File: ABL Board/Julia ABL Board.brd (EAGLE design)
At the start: 62.2 x 63.5 mm, 32 parts, among them Q1 MMBT4403, U2 LM317, U5 HX711, X1 LOADCELL 3, X2 LOADCELL 2, X3 LOADCELL 1, X4 INPUT, X8 ABL_LED

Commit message: generated ABL board gerbers
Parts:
- added U$2: FRACKTALLOGO, FracktalWorks_Eagle_Library:FRACKTALLOGO
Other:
- board text added: "Julia ABL Board V1.1"
- board text added: "Solder jumper for 12V operation"
- board text removed: "Julia ABL Board V1"
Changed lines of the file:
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@@
 <board>
 <plain>
-<wire x1="57.15" y1="88.9" x2="106.68" y2="88.9" width="0.1524" layer="51"/>
-<wire x1="106.68" y1="88.9" x2="106.68" y2="35.56" width="0.1524" layer="51"/>
-<wire x1="106.68" y1="35.56" x2="57.15" y2="35.56" width="0.1524" layer="51"/>
-<wire x1="57.15" y1="35.56" x2="57.15" y2="88.9" width="0.1524" layer="51"/>
 <hole x="57.15" y="88.9" drill="3"/>
 <hole x="106.68" y="88.9" drill="3"/>
@@
 <wire x1="50.8" y1="35.56" x2="50.8" y2="88.9" width="0.1524" layer="20"/>
 <wire x1="113.03" y1="35.56" x2="107.95" y2="30.48" width="0.1524" layer="20" curve="-90"/>
-<text x="71.12" y="33.02" size="1.778" layer="27">Julia ABL Board V1</text>
+<text x="70.5866" y="90.3478" size="1.778" layer="27">Julia ABL Board V1.1</text>
+<text x="82.5754" y="87.3506" size="1.016" layer="25">Solder jumper for 12V operation</text>
 </plain>
 <attributes>
@@
 <attribute name="VALUE" x="76.2" y="36.703" size="0.0254" layer="27"/>
 </element>
+<element name="U$2" library="FracktalWorks_Eagle_Library" package="FRACKTALLOGO" value="FRACKTALLOGO" x="79.502" y="32.1056" smashed="yes"/>
 </elements>
 <signals>
@@
 <mfgpreviewcolor name="substratecolor" color="0xFF786E46"/>
 </mfgpreviewcolors>
+<errors>
+</errors>
 </board>
 </drawing>

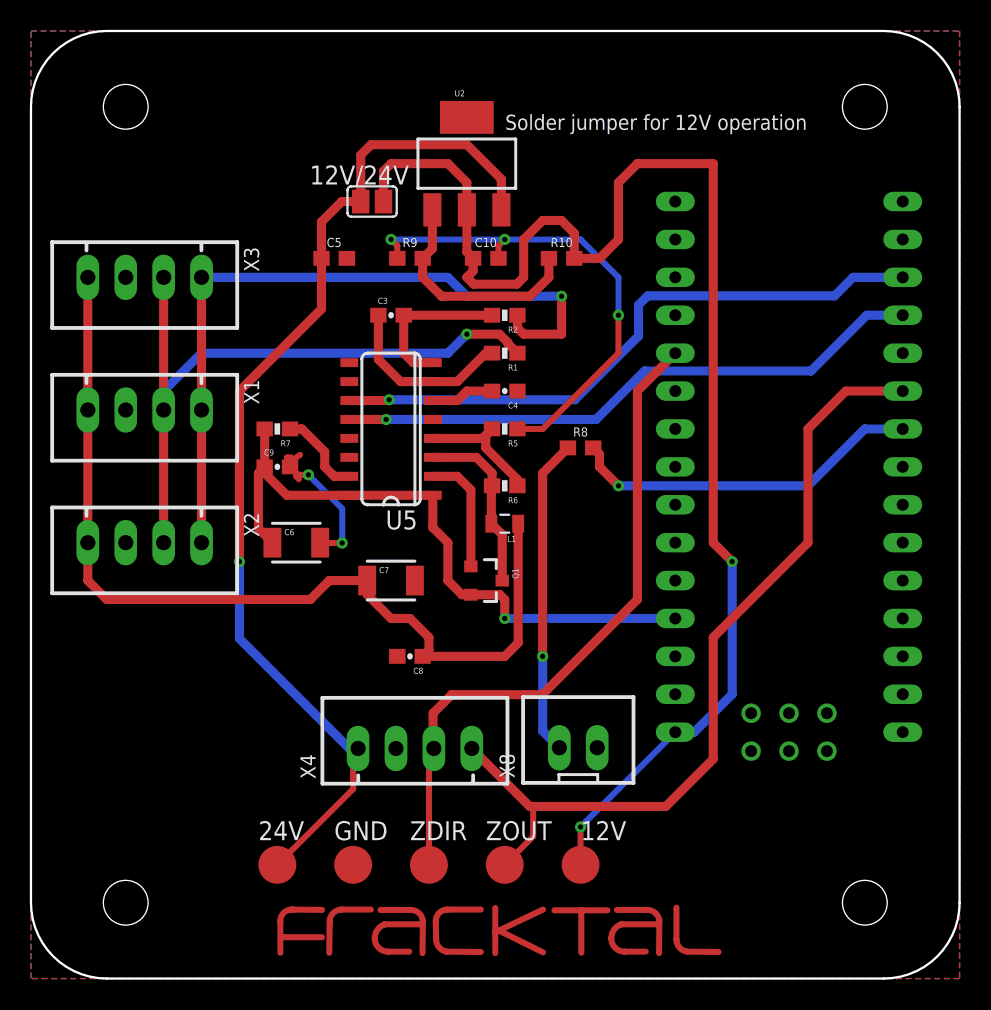
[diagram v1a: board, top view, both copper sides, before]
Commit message: Added LED to ABL board
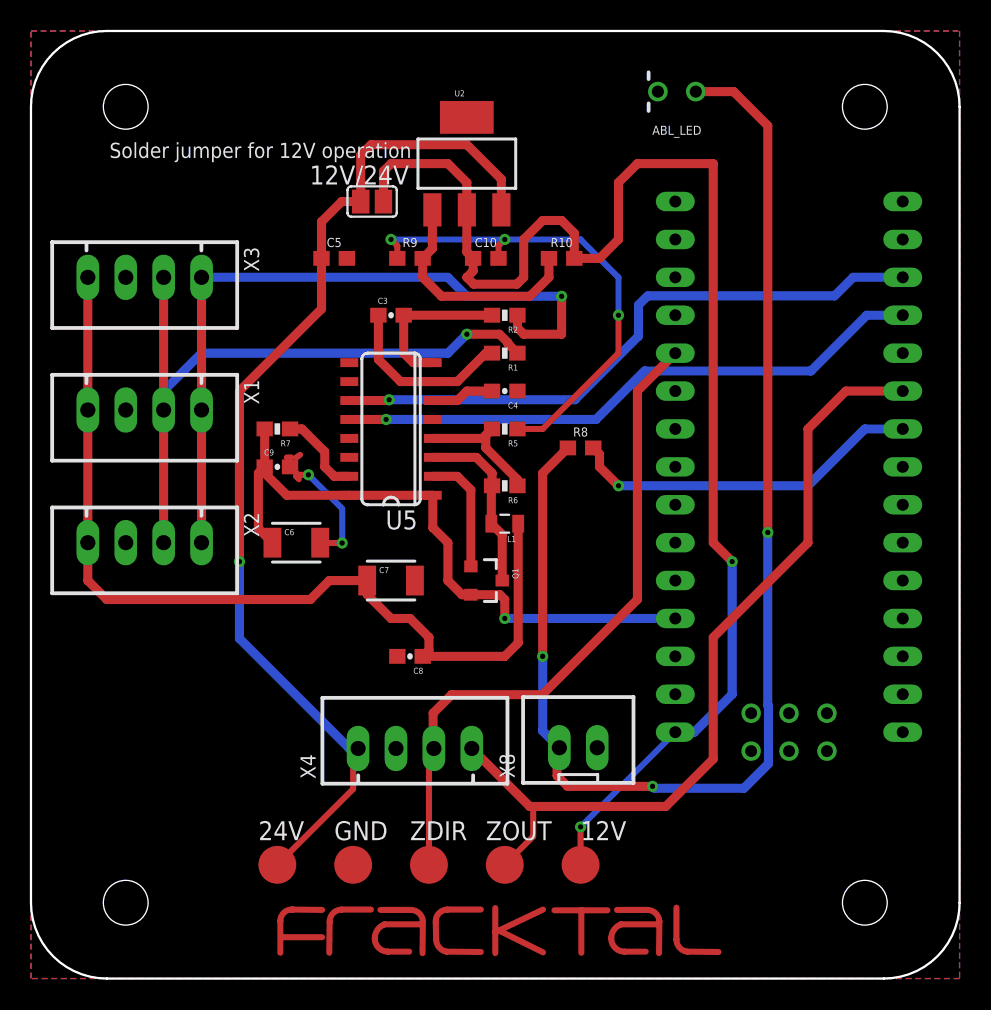
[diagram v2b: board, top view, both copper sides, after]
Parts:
- added ABL_LED: (no value), SparkFun-LED:LED_3MM-NS
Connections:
- net GND: now also ABL_LED.K
- net N$14: now also ABL_LED.A
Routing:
- net N$14: track 21.3 -> 86.9 mm, vias 1 -> 3
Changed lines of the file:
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@@
 <wire x1="50.8" y1="35.56" x2="50.8" y2="88.9" width="0.1524" layer="20"/>
 <wire x1="113.03" y1="35.56" x2="107.95" y2="30.48" width="0.1524" layer="20" curve="-90"/>
-<text x="70.5866" y="90.3478" size="1.778" layer="27">Julia ABL Board V1.1</text>
-<text x="82.5754" y="87.3506" size="1.016" layer="25">Solder jumper for 12V operation</text>
+<text x="63.5762" y="90.7288" size="1.778" layer="27">Julia ABL Board V1.1</text>
+<text x="56.0578" y="85.471" size="1.016" layer="25">Solder jumper for 12V operation</text>
 </plain>
 <attributes>
@@
 </element>
 <element name="U$2" library="FracktalWorks_Eagle_Library" package="FRACKTALLOGO" value="FRACKTALLOGO" x="79.502" y="32.1056" smashed="yes"/>
+<element name="ABL_LED" library="SparkFun-LED" package="LED_3MM-NS" value="" x="94.0816" y="89.916" smashed="yes" rot="R180">
+<attribute name="NAME" x="94.0816" y="87.63" size="0.6096" layer="25" font="vector" ratio="20" rot="R180" align="bottom-center"/>
+<attribute name="VALUE" x="94.0816" y="92.202" size="0.6096" layer="27" font="vector" ratio="20" rot="R180" align="top-center"/>
+</element>
 </elements>
 <signals>
@@
 <wire x1="67.945" y1="64.77" x2="68.236209375" y2="64.693803125" width="0.4064" layer="1"/>
 <wire x1="68.58" y1="65.405" x2="68.83745" y2="65.57769375" width="0.4064" layer="1"/>
+<contactref element="ABL_LED" pad="K"/>
 </signal>
 <signal name="SCK">
@@
 <wire x1="85.09" y1="52.07" x2="85.09" y2="47.0662" width="0.6096" layer="16"/>
 <wire x1="85.09" y1="47.0662" x2="86.2076" y2="45.9486" width="0.6096" layer="16"/>
+<contactref element="ABL_LED" pad="A"/>
+<wire x1="95.3516" y1="89.916" x2="97.8916" y2="89.916" width="0.6096" layer="1"/>
+<wire x1="100.1776" y1="87.63" x2="100.1776" y2="60.3758" width="0.6096" layer="1"/>
+<via x="100.1776" y="60.3758" extent="1-16" drill="0.35"/>
+<wire x1="100.1776" y1="60.3758" x2="100.1776" y2="48.78571875" width="0.6096" layer="16"/>
+<wire x1="100.1776" y1="48.78571875" x2="100.222" y2="48.74131875" width="0.6096" layer="16"/>
+<wire x1="100.222" y1="48.74131875" x2="100.222" y2="44.8754" width="0.6096" layer="16"/>
+<wire x1="100.222" y1="44.8754" x2="98.5774" y2="43.2308" width="0.6096" layer="16"/>
+<wire x1="98.5774" y1="43.2308" x2="92.583" y2="43.2308" width="0.6096" layer="16"/>
+<wire x1="92.583" y1="43.2308" x2="92.456" y2="43.3578" width="0.6096" layer="16"/>
+<via x="92.456" y="43.3578" extent="1-16" drill="0.35"/>
+<wire x1="92.456" y1="43.3578" x2="86.7664" y2="43.3578" width="0.6096" layer="1"/>
+<wire x1="86.7664" y1="43.3578" x2="86.0552" y2="44.069" width="0.6096" layer="1"/>
+<wire x1="86.0552" y1="44.069" x2="86.0552" y2="45.7962" width="0.6096" layer="1"/>
+<wire x1="86.0552" y1="45.7962" x2="86.2076" y2="45.9486" width="0.6096" layer="1"/>
+<wire x1="97.8916" y1="89.916" x2="100.1776" y2="87.63" width="0.6096" layer="1"/>
 </signal>
 <signal name="Z_DIR">
